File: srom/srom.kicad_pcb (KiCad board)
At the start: 2 copper layers, 83.3 x 76.1 mm, 31 parts, among them J1 Conn_01x03_Female, Q1 PN2222A, SW1 SW_SPST, U1 4075, U2 74LS245, U3 74LS245, U4 74LS245, U5 Pico-rp2040

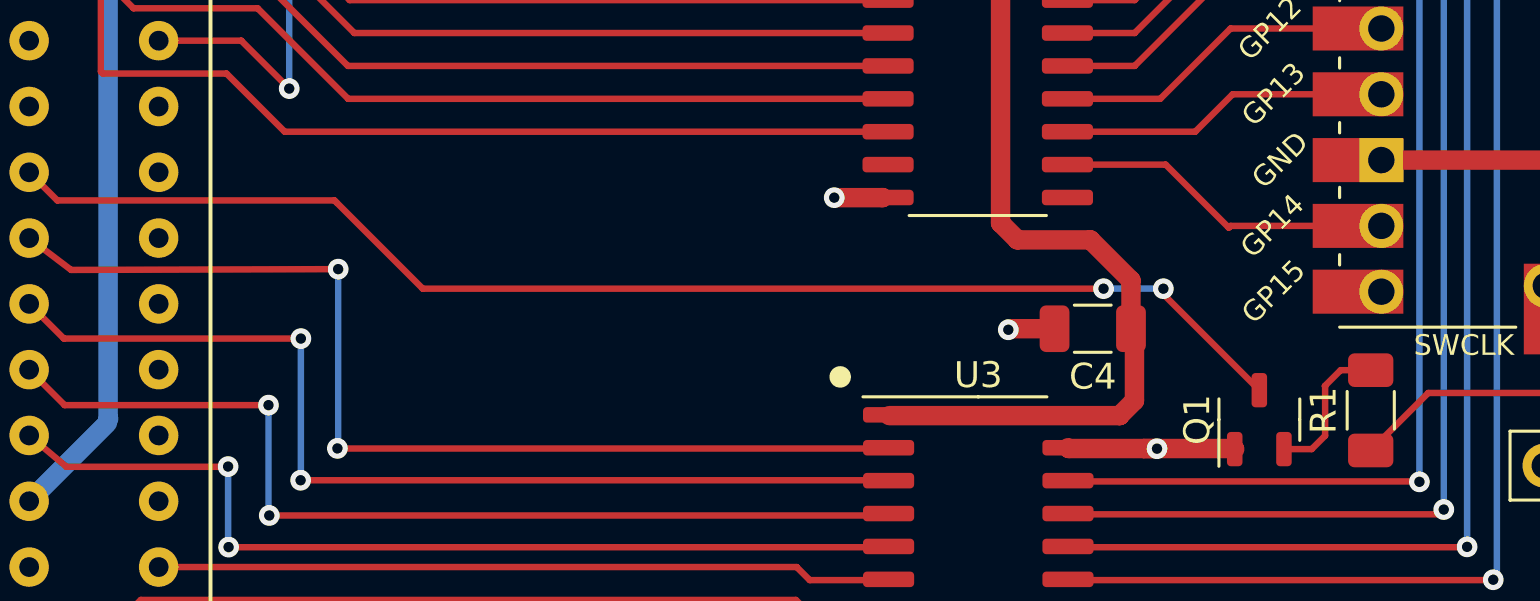
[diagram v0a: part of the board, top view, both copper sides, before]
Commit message: Add the /M1 line into the Pico so the IF1 ROM can be used
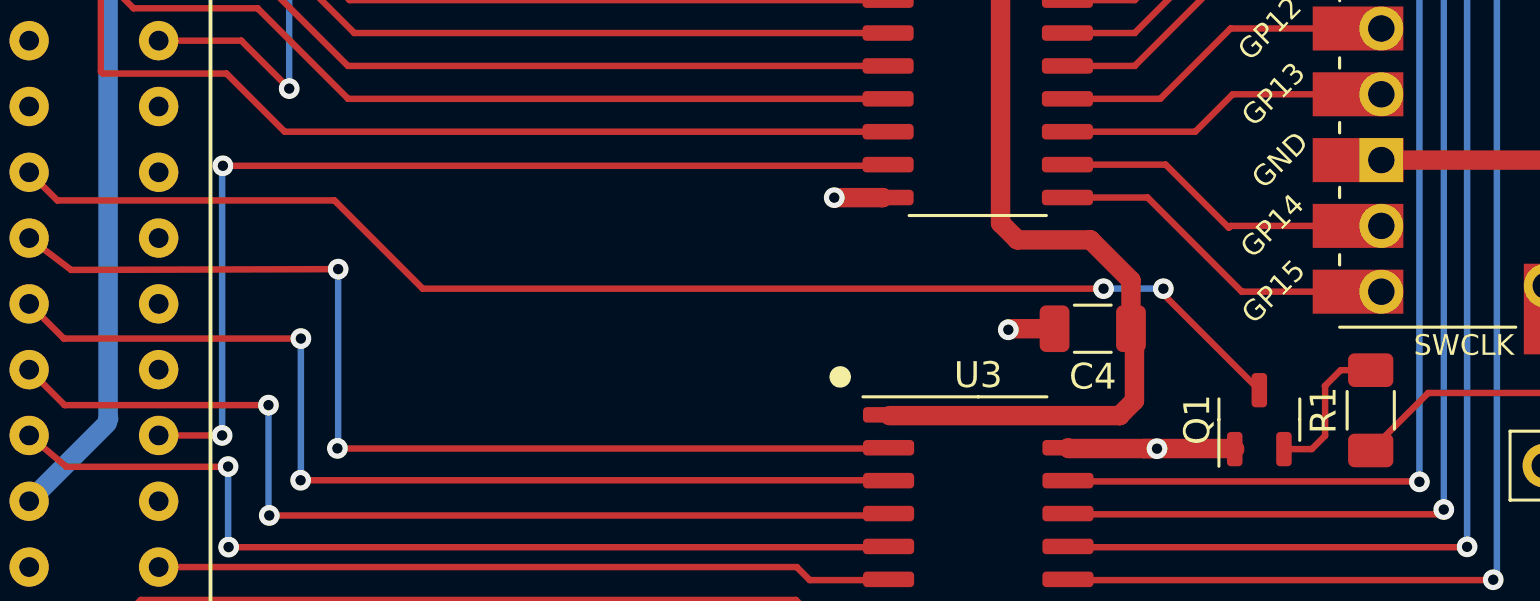
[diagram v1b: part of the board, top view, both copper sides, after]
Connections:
- U2 pad 11: unconnected-(U2-Pad11) -> M1
- U2 pad 9: unconnected-(U2-Pad9) -> ZXM1
- U5 pad 20: unconnected-(U5-Pad20) -> M1
- Z1 pad A24: unconnected-(Z1-PadA24) -> ZXM1
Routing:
- net ZXM1: track 0.00 -> 38.6 mm, vias 0 -> 2
- net M1: track 0.00 -> 13.6 mm
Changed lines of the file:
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@@
   (net 68 "unconnected-(Z1-PadA28)")
   (net 69 "unconnected-(Z1-PadA25)")
-  (net 70 "unconnected-(Z1-PadA24)")
+  (net 70 "ZXM1")
   (net 71 "unconnected-(Z1-PadA23)")
   (net 72 "unconnected-(Z1-PadA22)")
@@
   (net 86 "PICO_RESET_Z80")
   (net 87 "PICO_USER_INPUT")
-  (net 88 "unconnected-(U2-Pad9)")
-  (net 89 "unconnected-(U2-Pad11)")
-  (net 90 "unconnected-(U5-Pad20)")
-  (net 91 "unconnected-(Z1-PadA19)")
+  (net 88 "M1")
+  (net 89 "unconnected-(Z1-PadA19)")
   (footprint "" (layer "F.Cu")
     (at 48.2 122)
@@
       (net 11 "ZXA3") (pinfunction "A6") (pintype "tri_state"))
     (pad "9" smd roundrect (at -3.4625 4.445) (size 1.975 0.6) (layers "F.Cu" "F.Paste" "F.Mask") (roundrect_rratio 0.25)
-      (net 88 "unconnected-(U2-Pad9)") (pinfunction "A7") (pintype "tri_state+no_connect"))
+      (net 70 "ZXM1") (pinfunction "A7") (pintype "tri_state"))
     (pad "10" smd roundrect (at -3.4625 5.715) (size 1.975 0.6) (layers "F.Cu" "F.Paste" "F.Mask") (roundrect_rratio 0.25)
       (net 2 "GND") (pinfunction "GND") (pintype "power_in"))
     (pad "11" smd roundrect (at 3.4625 5.715) (size 1.975 0.6) (layers "F.Cu" "F.Paste" "F.Mask") (roundrect_rratio 0.25)
-      (net 89 "unconnected-(U2-Pad11)") (pinfunction "B7") (pintype "tri_state+no_connect"))
+      (net 88 "M1") (pinfunction "B7") (pintype "tri_state"))
     (pad "12" smd roundrect (at 3.4625 4.445) (size 1.975 0.6) (layers "F.Cu" "F.Paste" "F.Mask") (roundrect_rratio 0.25)
       (net 18 "A3") (pinfunction "B6") (pintype "tri_state"))
@@
       (net 75 "ZXRD") (pinfunction "~{RD}") (pintype "bidirectional"))
     (pad "A19" thru_hole circle (at 11.43 -5 270) (size 1.524 1.524) (drill 0.762) (layers *.Cu *.Mask)
-      (net 91 "unconnected-(Z1-PadA19)") (pinfunction "~{WR}") (pintype "bidirectional+no_connect"))
+      (net 89 "unconnected-(Z1-PadA19)") (pinfunction "~{WR}") (pintype "bidirectional+no_connect"))
     (pad "A20" thru_hole circle (at 13.97 -5 270) (size 1.524 1.524) (drill 0.762) (layers *.Cu *.Mask)
       (net 74 "unconnected-(Z1-PadA20)") (pinfunction "-5V") (pintype "input+no_connect"))
@@
       (net 71 "unconnected-(Z1-PadA23)") (pinfunction "+12VAC") (pintype "input+no_connect"))
     (pad "A24" thru_hole circle (at 24.13 -5 270) (size 1.524 1.524) (drill 0.762) (layers *.Cu *.Mask)
-      (net 70 "unconnected-(Z1-PadA24)") (pinfunction "~{M1}") (pintype "input+no_connect"))
+      (net 70 "ZXM1") (pinfunction "~{M1}") (pintype "input"))
     (pad "A25" thru_hole circle (at 26.67 -5 270) (size 1.524 1.524) (drill 0.762) (layers *.Cu *.Mask)
       (net 69 "unconnected-(Z1-PadA25)") (pinfunction "~{RFSH}") (pintype "input+no_connect"))
@@
       (net 18 "A3") (pinfunction "GPIO14") (pintype "bidirectional"))
     (pad "20" thru_hole oval (at -8.89 24.13) (size 1.7 1.7) (drill 1.02) (layers *.Cu *.Mask)
-      (net 90 "unconnected-(U5-Pad20)") (pinfunction "GPIO15") (pintype "bidirectional+no_connect"))
+      (net 88 "M1") (pinfunction "GPIO15") (pintype "bidirectional"))
     (pad "20" smd rect (at -8.89 24.13) (size 3.5 1.7) (drill (offset -0.9 0)) (layers "F.Cu" "F.Mask")
-      (net 90 "unconnected-(U5-Pad20)") (pinfunction "GPIO15") (pintype "bidirectional+no_connect"))
+      (net 88 "M1") (pinfunction "GPIO15") (pintype "bidirectional"))
     (pad "21" smd rect (at 8.89 24.13) (size 3.5 1.7) (drill (offset 0.9 0)) (layers "F.Cu" "F.Mask")
       (net 32 "A11") (pinfunction "GPIO16") (pintype "bidirectional"))
@@
   (segment (start 54.35 53.64) (end 54.35 79.22) (width 0.25) (layer "B.Cu") (net 65))
   (segment (start 54.35 79.22) (end 54.67 79.54) (width 0.25) (layer "B.Cu") (net 65))
+  (segment (start 33.15 112) (end 35.6 112) (width 0.25) (layer "F.Cu") (net 70))
+  (segment (start 35.63 101.59) (end 61.2625 101.59) (width 0.25) (layer "F.Cu") (net 70))
+  (segment (start 61.2625 101.59) (end 61.3075 101.545) (width 0.25) (layer "F.Cu") (net 70))
+  (via (at 35.63 101.59) (size 0.8) (drill 0.4) (layers "F.Cu" "B.Cu") (net 70))
+  (via (at 35.6 112) (size 0.8) (drill 0.4) (layers "F.Cu" "B.Cu") (net 70))
+  (segment (start 35.6 112) (end 35.6 101.62) (width 0.25) (layer "B.Cu") (net 70))
+  (segment (start 35.6 101.62) (end 35.63 101.59) (width 0.25) (layer "B.Cu") (net 70))
   (segment (start 36.34 96.76) (end 38.19 98.61) (width 0.25) (layer "F.Cu") (net 75))
   (segment (start 55.75 86.27) (end 55.81 86.33) (width 0.25) (layer "F.Cu") (net 75))
@@
   (segment (start 100.59 78.51) (end 100.86 78.51) (width 0.25) (layer "B.Cu") (net 87))
   (segment (start 100.86 78.51) (end 103.09 76.28) (width 0.25) (layer "B.Cu") (net 87))
+  (segment (start 74.98 106.45) (end 80.35 106.45) (width 0.25) (layer "F.Cu") (net 88))
+  (segment (start 71.325 102.815) (end 74.97 106.46) (width 0.25) (layer "F.Cu") (net 88))
+  (segment (start 68.2325 102.815) (end 71.325 102.815) (width 0.25) (layer "F.Cu") (net 88))
+  (segment (start 74.97 106.46) (end 74.98 106.45) (width 0.25) (layer "F.Cu") (net 88))
   (zone (net 2) (net_name "GND") (layers F&B.Cu) (hatch edge 0.508)
     (connect_pads (clearance 0.508))

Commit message: v1.2 schematic and layout complete
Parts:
- Q1: value PN2222A -> PMBT2222A; footprint Package_TO_SOT_SMD:SOT-23-3 -> Package_TO_SOT_SMD:TSOT-23_HandSoldering
- SW1: footprint Button_Switch_THT:SW_PUSH_6mm_H4.3mm -> Button_Switch_THT:SW_Tactile_SKHH_Angled
- moved SW1 6.00 mm to (101.9, 118.4), turned to -90 degrees
- moved Q1 1.87 mm to (74.6, 109.8), turned to 180 degrees
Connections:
- Q1 pad 1: GND -> Net-(R1-Pad2)
- Q1 pad 2: Net-(Q1-Pad2) -> GND
- R1 pad 2: Net-(Q1-Pad2) -> Net-(R1-Pad2)
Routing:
- net Net-(Q1-Pad2): track 5.75 -> 0.00 mm
- net Net-(R1-Pad2): track 0.00 -> 4.36 mm
- net +3V3: track 196.8 -> 193.8 mm
- net GND: track 86.2 -> 84.4 mm, vias 18 -> 19
- net ZXRESET: track 51.1 -> 49.5 mm
- net PICO_USER_INPUT: track 75.5 -> 74.2 mm
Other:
- board text added: "github.com/derekfountain/zx-spectrum-pico-rom v1.2"
- board text removed: "github.com/derekfountain/zx-spectrum-pico-rom v1.1"
